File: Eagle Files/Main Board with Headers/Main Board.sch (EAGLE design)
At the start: 52 parts, among them IC1 FT232RL, Y1 16MHz, Y2 16 MHZ

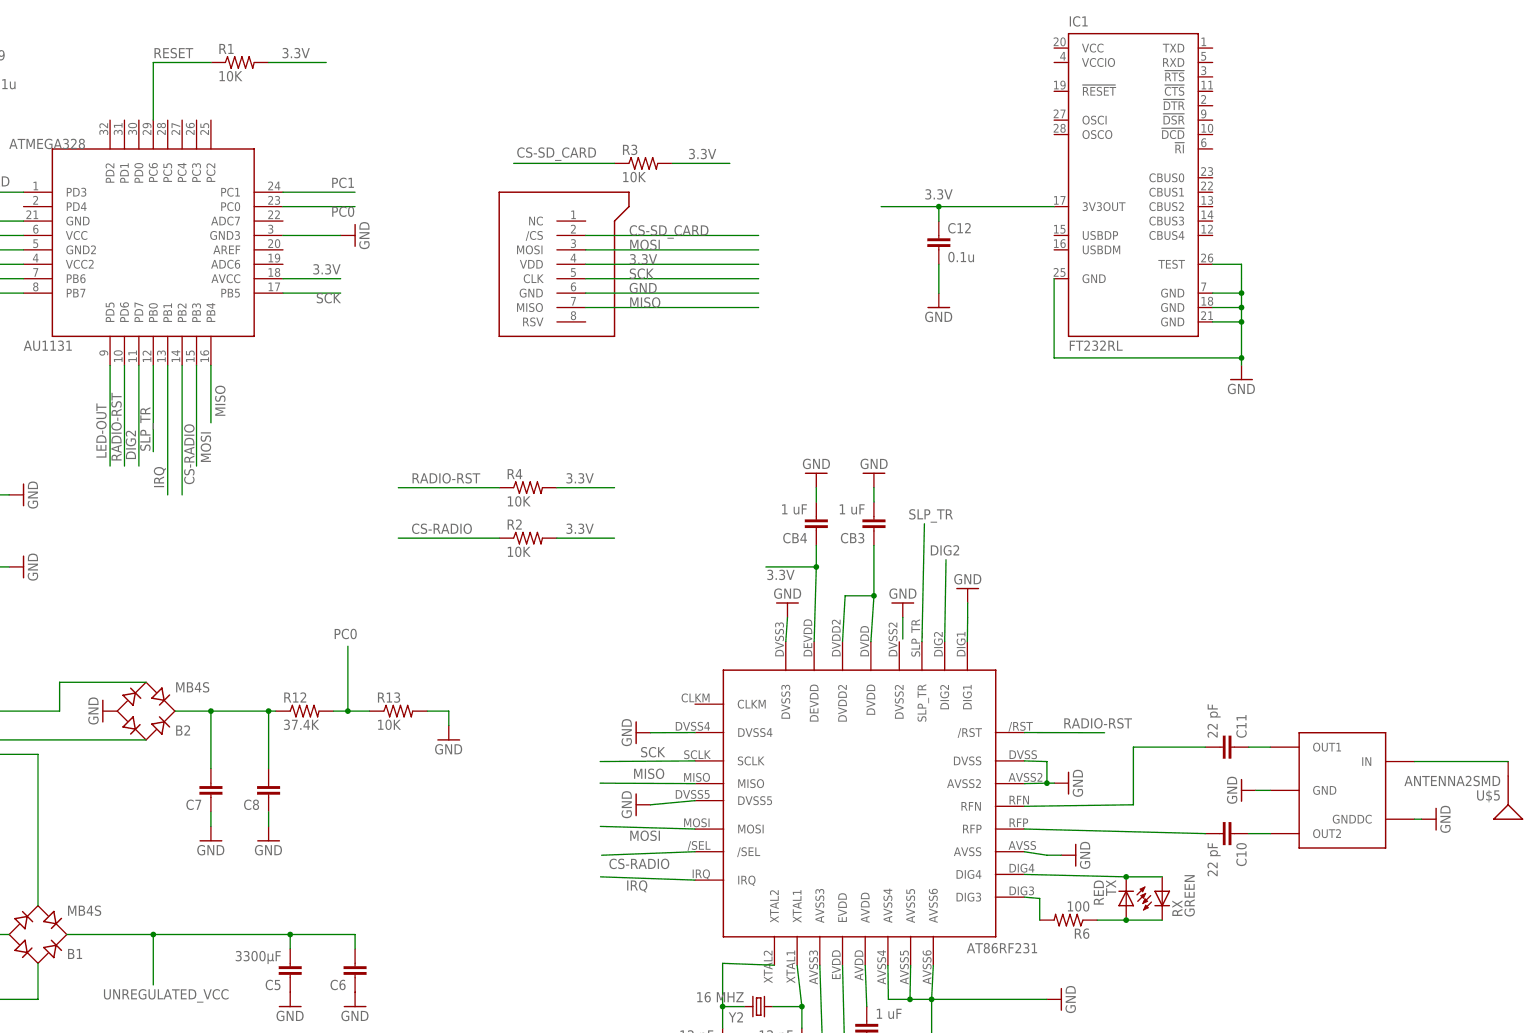
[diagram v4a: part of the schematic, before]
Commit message: Added USB to Serial Capability to the board.
--Arthur

git-svn-id: http://cd-net.net/CPE496/trunk@122 05b6d0e0-c345-4a8e-a5b7-579c8bd0b646
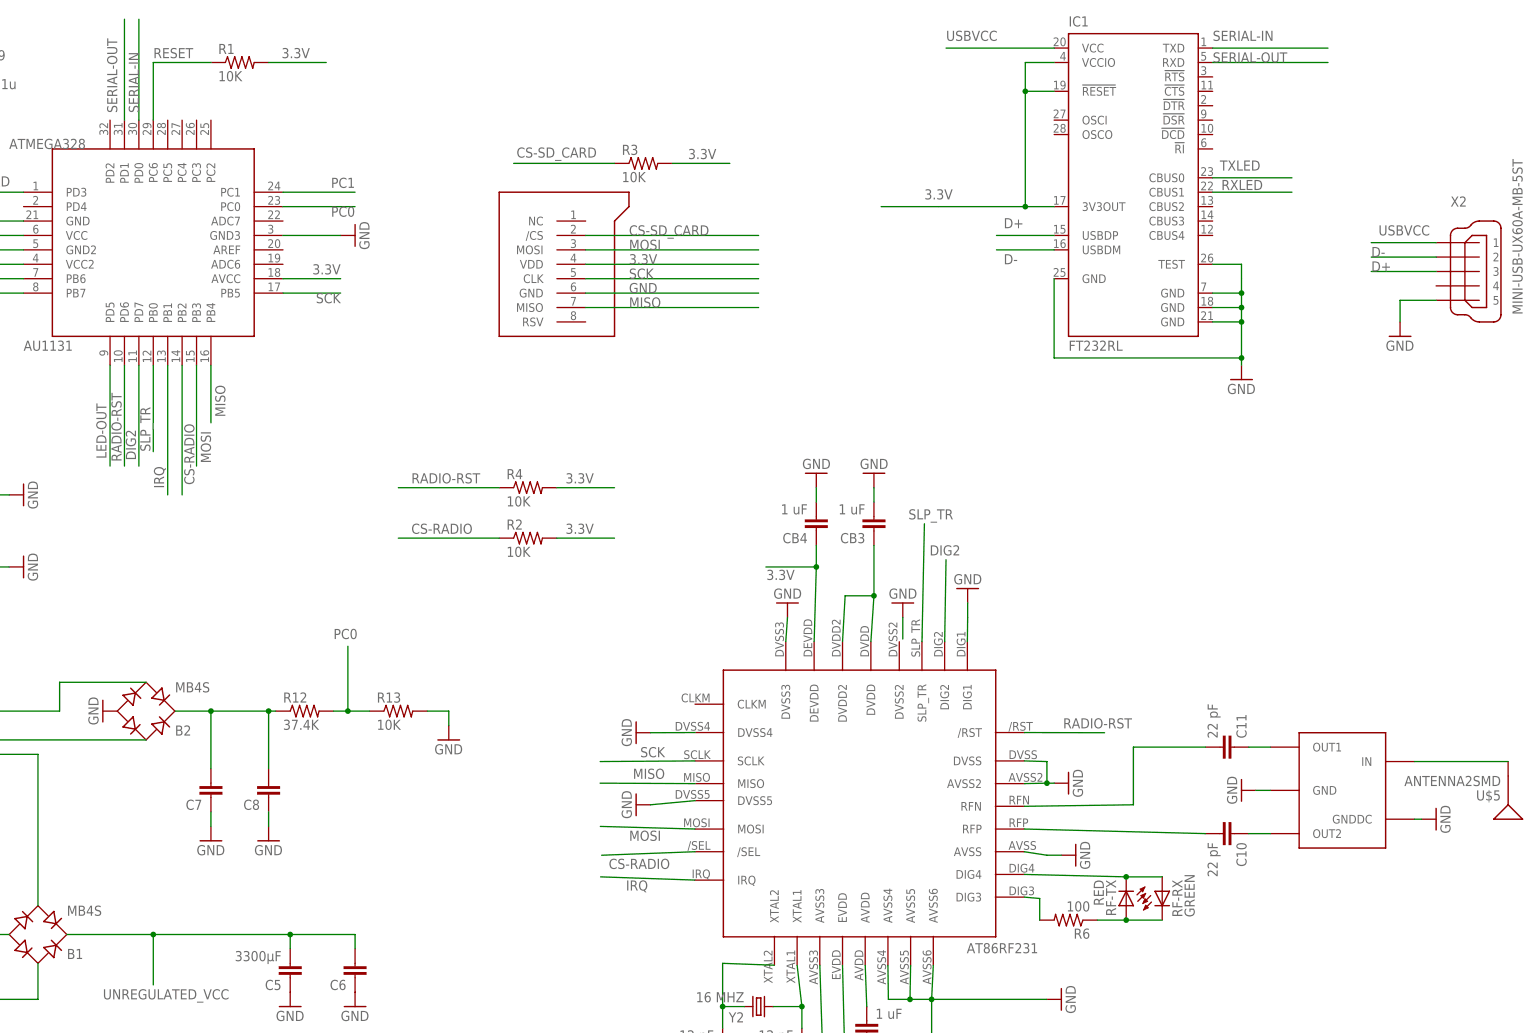
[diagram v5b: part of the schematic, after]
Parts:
- removed C12: 0.1u, SparkFun:CAP0603-CAP
- added X2: MINI-USB-UX60A-MB-5ST, con-hirose:MINI-USB-UX60A-MB-5ST
- renumbered RX to RF-RX, TX to RF-TX
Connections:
- new net D+: IC1.USBDP, X2.3
- new net D-: IC1.USBDM, X2.2
- new net RXLED: IC1.CBUS1
- new net SERIAL-IN: IC1.TXD, U$2.PD0
- new net SERIAL-OUT: IC1.RXD, U$2.PD1
- new net TXLED: IC1.CBUS0
- new net USBVCC: IC1.VCC, X2.1
- net 3.3V: now also IC1.!RESET, IC1.VCCIO; no longer C12.1
- net GND: now also X2.5; no longer C12.2
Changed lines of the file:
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@@
 <setting verticaltext="up"/>
 </settings>
-<grid distance="0.05" unitdist="inch" unit="inch" style="lines" multiple="1" display="yes" altdistance="0.005" altunitdist="inch" altunit="inch"/>
+<grid distance="0.05" unitdist="inch" unit="mil" style="lines" multiple="1" display="yes" altdistance="0.005" altunitdist="inch" altunit="inch"/>
 <layers>
 <layer number="1" name="Top" color="4" fill="1" visible="no" active="no"/>
@@
 <part name="GND27" library="supply1" deviceset="GND" device=""/>
 <part name="GND28" library="supply1" deviceset="GND" device=""/>
-<part name="TX" library="SparkFun" deviceset="LED" device="0603" value="RED"/>
-<part name="RX" library="SparkFun" deviceset="LED" device="0603" value="GREEN"/>
+<part name="RF-TX" library="SparkFun" deviceset="LED" device="0603" value="RED"/>
+<part name="RF-RX" library="SparkFun" deviceset="LED" device="0603" value="GREEN"/>
 <part name="GND29" library="supply1" deviceset="GND" device=""/>
 <part name="R6" library="SparkFun" deviceset="RESISTOR" device="0603-RES" value="100"/>
@@
 <part name="R4" library="SparkFun" deviceset="RESISTOR" device="0603-RES" value="10K"/>
 <part name="GND11" library="supply1" deviceset="GND" device=""/>
-<part name="C12" library="SparkFun" deviceset="CAP" device="0603-CAP" value="0.1u"/>
-<part name="GND32" library="supply1" deviceset="GND" device=""/>
 <part name="IC1" library="ftdichip" deviceset="FT232R" device="L"/>
+<part name="X2" library="con-hirose" deviceset="MINI-USB-" device="UX60A-MB-5ST"/>
+<part name="GND33" library="supply1" deviceset="GND" device=""/>
 </parts>
 <sheets>
@@
 <instance part="GND27" gate="1" x="82.55" y="-19.05" rot="R270"/>
 <instance part="GND28" gate="1" x="82.55" y="-6.35" rot="R270"/>
-<instance part="TX" gate="G$1" x="168.91" y="-36.83" rot="R180"/>
-<instance part="RX" gate="G$1" x="175.26" y="-34.29"/>
+<instance part="RF-TX" gate="G$1" x="168.91" y="-36.83" rot="R180"/>
+<instance part="RF-RX" gate="G$1" x="175.26" y="-34.29"/>
 <instance part="GND29" gate="1" x="160.02" y="-27.94" rot="R90"/>
 <instance part="R6" gate="G$1" x="158.75" y="-39.37" rot="R180"/>
@@
 <instance part="R4" gate="G$1" x="63.5" y="36.83"/>
 <instance part="GND11" gate="1" x="189.23" y="55.88"/>
-<instance part="C12" gate="G$1" x="135.89" y="78.74"/>
-<instance part="GND32" gate="1" x="135.89" y="68.58"/>
 <instance part="IC1" gate="1" x="168.91" y="91.44"/>
+<instance part="X2" gate="G$1" x="228.6" y="74.93"/>
+<instance part="GND33" gate="1" x="217.17" y="63.5"/>
 </instances>
 <busses>
@@
 </segment>
 <segment>
-<pinref part="GND32" gate="1" pin="GND"/>
-<pinref part="C12" gate="G$1" pin="2"/>
-<wire x1="135.89" y1="71.12" x2="135.89" y2="76.2" width="0.1524" layer="91"/>
+<pinref part="X2" gate="G$1" pin="5"/>
+<wire x1="223.52" y1="69.85" x2="217.17" y2="69.85" width="0.1524" layer="91"/>
+<pinref part="GND33" gate="1" pin="GND"/>
+<wire x1="217.17" y1="66.04" x2="217.17" y2="69.85" width="0.1524" layer="91"/>
 </segment>
 </net>
@@
 </segment>
 <segment>
-<wire x1="156.21" y1="86.36" x2="135.89" y2="86.36" width="0.1524" layer="91"/>
+<wire x1="156.21" y1="86.36" x2="151.13" y2="86.36" width="0.1524" layer="91"/>
 <label x="133.35" y="87.63" size="1.778" layer="95"/>
-<pinref part="C12" gate="G$1" pin="1"/>
+<wire x1="151.13" y1="86.36" x2="135.89" y2="86.36" width="0.1524" layer="91"/>
 <wire x1="135.89" y1="86.36" x2="125.73" y2="86.36" width="0.1524" layer="91"/>
-<wire x1="135.89" y1="83.82" x2="135.89" y2="86.36" width="0.1524" layer="91"/>
-<junction x="135.89" y="86.36"/>
+<pinref part="IC1" gate="1" pin="VCCIO"/>
+<wire x1="156.21" y1="111.76" x2="151.13" y2="111.76" width="0.1524" layer="91"/>
+<wire x1="151.13" y1="111.76" x2="151.13" y2="106.68" width="0.1524" layer="91"/>
+<junction x="151.13" y="86.36"/>
+<pinref part="IC1" gate="1" pin="!RESET"/>
+<wire x1="151.13" y1="106.68" x2="151.13" y2="86.36" width="0.1524" layer="91"/>
+<wire x1="156.21" y1="106.68" x2="151.13" y2="106.68" width="0.1524" layer="91"/>
+<junction x="151.13" y="106.68"/>
 </segment>
 </net>
@@
 <segment>
 <pinref part="U$3" gate="G$1" pin="DIG4"/>
-<pinref part="TX" gate="G$1" pin="C"/>
+<pinref part="RF-TX" gate="G$1" pin="C"/>
 <wire x1="150.92" y1="-31.32" x2="168.91" y2="-31.75" width="0.1524" layer="91"/>
-<pinref part="RX" gate="G$1" pin="A"/>
+<pinref part="RF-RX" gate="G$1" pin="A"/>
 <wire x1="168.91" y1="-31.75" x2="175.26" y2="-31.75" width="0.1524" layer="91"/>
 <junction x="168.91" y="-31.75"/>
@@
 <net name="N$14" class="0">
 <segment>
-<pinref part="TX" gate="G$1" pin="A"/>
-<pinref part="RX" gate="G$1" pin="C"/>
+<pinref part="RF-TX" gate="G$1" pin="A"/>
+<pinref part="RF-RX" gate="G$1" pin="C"/>
 <wire x1="168.91" y1="-39.37" x2="175.26" y2="-39.37" width="0.1524" layer="91"/>
 <pinref part="R6" gate="G$1" pin="1"/>
@@
 </segment>
 </net>
+<net name="SERIAL-OUT" class="0">
+<segment>
+<pinref part="U$2" gate="G$1" pin="PD1"/>
+<wire x1="-7.62" y1="101.6" x2="-7.62" y2="119.38" width="0.1524" layer="91"/>
+<label x="-8.89" y="102.87" size="1.778" layer="95" rot="R90"/>
+</segment>
+<segment>
+<pinref part="IC1" gate="1" pin="RXD"/>
+<wire x1="184.15" y1="111.76" x2="204.47" y2="111.76" width="0.1524" layer="91"/>
+<label x="184.15" y="111.76" size="1.778" layer="95"/>
+</segment>
+</net>
+<net name="SERIAL-IN" class="0">
+<segment>
+<pinref part="U$2" gate="G$1" pin="PD0"/>
+<wire x1="-5.08" y1="101.6" x2="-5.08" y2="119.38" width="0.1524" layer="91"/>
+<label x="-5.08" y="102.87" size="1.778" layer="95" rot="R90"/>
+</segment>
+<segment>
+<pinref part="IC1" gate="1" pin="TXD"/>
+<wire x1="184.15" y1="114.3" x2="204.47" y2="114.3" width="0.1524" layer="91"/>
+<label x="184.15" y="115.57" size="1.778" layer="95"/>
+</segment>
+</net>
+<net name="RXLED" class="0">
+<segment>
+<pinref part="IC1" gate="1" pin="CBUS1"/>
+<wire x1="184.15" y1="88.9" x2="198.12" y2="88.9" width="0.1524" layer="91"/>
+<label x="185.674" y="89.281" size="1.778" layer="95"/>
+</segment>
+</net>
+<net name="TXLED" class="0">
+<segment>
+<pinref part="IC1" gate="1" pin="CBUS0"/>
+<wire x1="184.15" y1="91.44" x2="198.12" y2="91.44" width="0.1524" layer="91"/>
+<label x="185.42" y="92.71" size="1.778" layer="95"/>
+</segment>
+</net>
+<net name="USBVCC" class="0">
+<segment>
+<pinref part="IC1" gate="1" pin="VCC"/>
+<wire x1="156.21" y1="114.3" x2="137.16" y2="114.3" width="0.1524" layer="91"/>
+<label x="137.16" y="115.57" size="1.778" layer="95"/>
+</segment>
+<segment>
+<pinref part="X2" gate="G$1" pin="1"/>
+<wire x1="223.52" y1="80.01" x2="212.09" y2="80.01" width="0.1524" layer="91"/>
+<label x="213.36" y="81.28" size="1.778" layer="95"/>
+</segment>
+</net>
+<net name="D+" class="0">
+<segment>
+<pinref part="IC1" gate="1" pin="USBDP"/>
+<wire x1="156.21" y1="81.28" x2="146.05" y2="81.28" width="0.1524" layer="91"/>
+<label x="147.32" y="82.55" size="1.778" layer="95"/>
+</segment>
+<segment>
+<pinref part="X2" gate="G$1" pin="3"/>
+<wire x1="223.52" y1="74.93" x2="212.09" y2="74.93" width="0.1524" layer="91"/>
+<label x="212.09" y="74.93" size="1.778" layer="95"/>
+</segment>
+</net>
+<net name="D-" class="0">
+<segment>
+<pinref part="IC1" gate="1" pin="USBDM"/>
+<wire x1="156.21" y1="78.74" x2="146.05" y2="78.74" width="0.1524" layer="91"/>
+<label x="147.32" y="76.2" size="1.778" layer="95"/>
+</segment>
+<segment>
+<pinref part="X2" gate="G$1" pin="2"/>
+<wire x1="223.52" y1="77.47" x2="212.09" y2="77.47" width="0.1524" layer="91"/>
+<label x="212.09" y="77.47" size="1.778" layer="95"/>
+</segment>
+</net>

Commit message: Updated the Board we're having made.
--Arthur

git-svn-id: http://cd-net.net/CPE496/trunk@127 05b6d0e0-c345-4a8e-a5b7-579c8bd0b646
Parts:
- removed U$3: AT86RF231(RADIO)AT86RF231, group10:AT86RF231(RADIO)AT86RF231
- removed U$4: WE-BAL, group10:WE-BAL
- removed U$5: ANTENNA2SMD, SparkFun:ANTENNA2SMD
- added ANTENNA: ANTENNA2SMD, SparkFun:ANTENNA2SMD
- added AT86RF231: AT86RF231(RADIO)AT86RF231, group10:AT86RF231(RADIO)AT86RF231
- added BALUN: WE-BAL, group10:WE-BAL
- added C12: 10 nF, SparkFun:CAP0603-CAP
- ACHOT, ACNEU, ACOUT: device wirepad:3,81/1,4 -> group10:PTH3MM
- C3, C4: value 22p -> 22 pF
- MT2201: value (none) -> 115V -> 5V
- RF-RX: value GREEN -> Green
- RF-TX: value RED -> Red
- Y1: value 16MHz -> 16 MHZ
- renumbered U$1 to MICROSD, U$2 to ATMEGA328
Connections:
- removed net RXLED: IC1.CBUS1
- removed net TXLED: IC1.CBUS0
- new net 3.3V1: 3.3V_REGULATOR.BYPASS, C12.2
- net 3.3V: now also AT86RF231.DEVDD, AT86RF231.EVDD, IC1.3V3OUT; no longer U$3.DEVDD, U$3.EVDD
- net CS-RADIO: now also AT86RF231./SEL; no longer U$3./SEL
- net DIG2: now also AT86RF231.DIG2; no longer U$3.DIG2
- net GND: now also AT86RF231.AVSS, AT86RF231.AVSS2, AT86RF231.AVSS3, AT86RF231.AVSS4, AT86RF231.AVSS5, AT86RF231.AVSS6, AT86RF231.DIG1, AT86RF231.DVSS, AT86RF231.DVSS2, AT86RF231.DVSS3, AT86RF231.DVSS4, AT86RF231.DVSS5, AT86RF231.GND, BALUN.GND, BALUN.GNDDC, C12.1; no longer U$3.AVSS, U$3.AVSS2, U$3.AVSS3, U$3.AVSS4, U$3.AVSS5, U$3.AVSS6, U$3.DIG1, U$3.DVSS, U$3.DVSS3, U$3.DVSS4, U$3.DVSS5, U$4.GND, U$4.GNDDC
- net IRQ: now also AT86RF231.IRQ; no longer U$3.IRQ
- net MISO: now also AT86RF231.MISO; no longer U$3.MISO
- net MOSI: now also AT86RF231.MOSI; no longer U$3.MOSI
- net N$10: now also AT86RF231.AVDD; no longer U$3.AVDD
- net N$11: now also AT86RF231.XTAL1; no longer U$3.XTAL1
- net N$12: now also AT86RF231.XTAL2; no longer U$3.XTAL2
- net N$13: now also AT86RF231.DIG4; no longer U$3.DIG4
- net N$15: now also AT86RF231.DIG3; no longer U$3.DIG3
- net N$16: now also BALUN.OUT2; no longer U$4.OUT2
- net N$17: now also BALUN.OUT1; no longer U$4.OUT1
- net N$18: now also AT86RF231.RFN; no longer U$3.RFN
- net N$19: now also AT86RF231.RFP; no longer U$3.RFP
- net N$20: now also ANTENNA.SIGNAL, BALUN.IN; no longer U$4.IN, U$5.SIGNAL
- net N$8: now also AT86RF231.DVDD, AT86RF231.DVDD2; no longer U$3.DVDD, U$3.DVDD2
- net RADIO-RST: now also AT86RF231./RST; no longer U$3./RST
- net SCK: now also AT86RF231.SCLK; no longer U$3.SCLK
- net SLP_TR: now also AT86RF231.SLP_TR; no longer U$3.SLP_TR
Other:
- moved on the sheet: ACHOT, ACNEU, ACOUT, C10, C11, CB1, CB2, CB3, CB4, CX1, R6, RF-RX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
